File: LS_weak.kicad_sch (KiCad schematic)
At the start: 6 parts, among them Q24 AO3400A

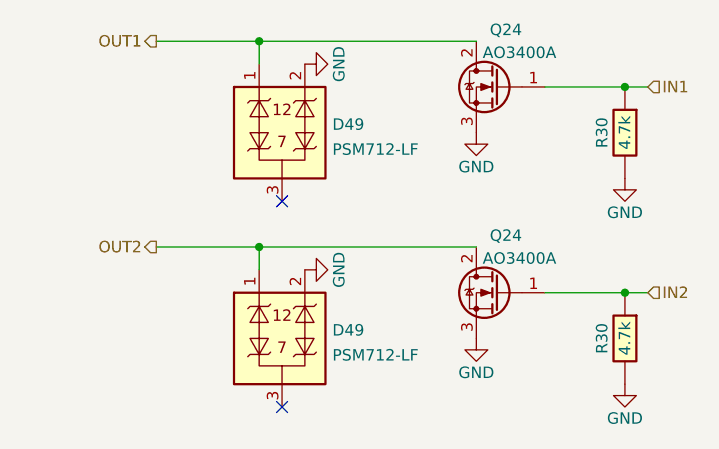
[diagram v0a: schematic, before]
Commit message: 0.04 revB begins
Added pullup resistor so tach works
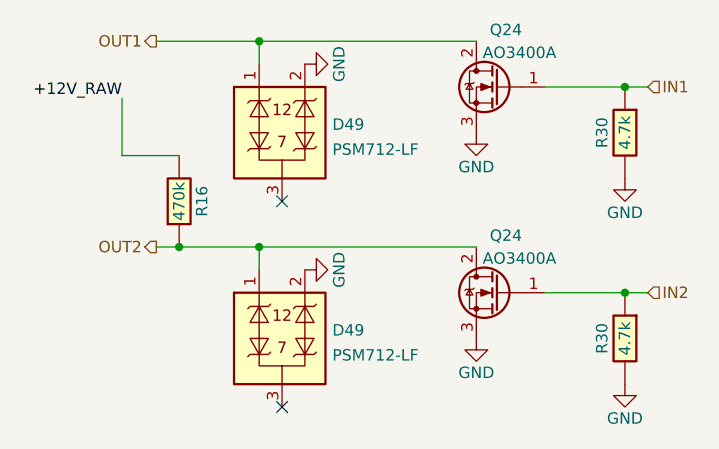
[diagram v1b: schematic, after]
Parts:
- added R16: 470k, hellen-one-common:R0603, symbol hellen-one-common:Res
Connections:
- net OUT2: now also R16.1
- new net +12V_RAW: R16.2
